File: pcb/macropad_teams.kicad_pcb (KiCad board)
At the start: 2 copper layers, 140 x 72.5 mm, 32 parts, among them J1 Conn_01x04, SW1 SW_Push, SW10 SW_Push, SW11 SW_Push, SW12 SW_Push, SW13 SW_Push, SW14 SW_Push, SW2 SW_Push, SW3 SW_Push, SW4 SW_Push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

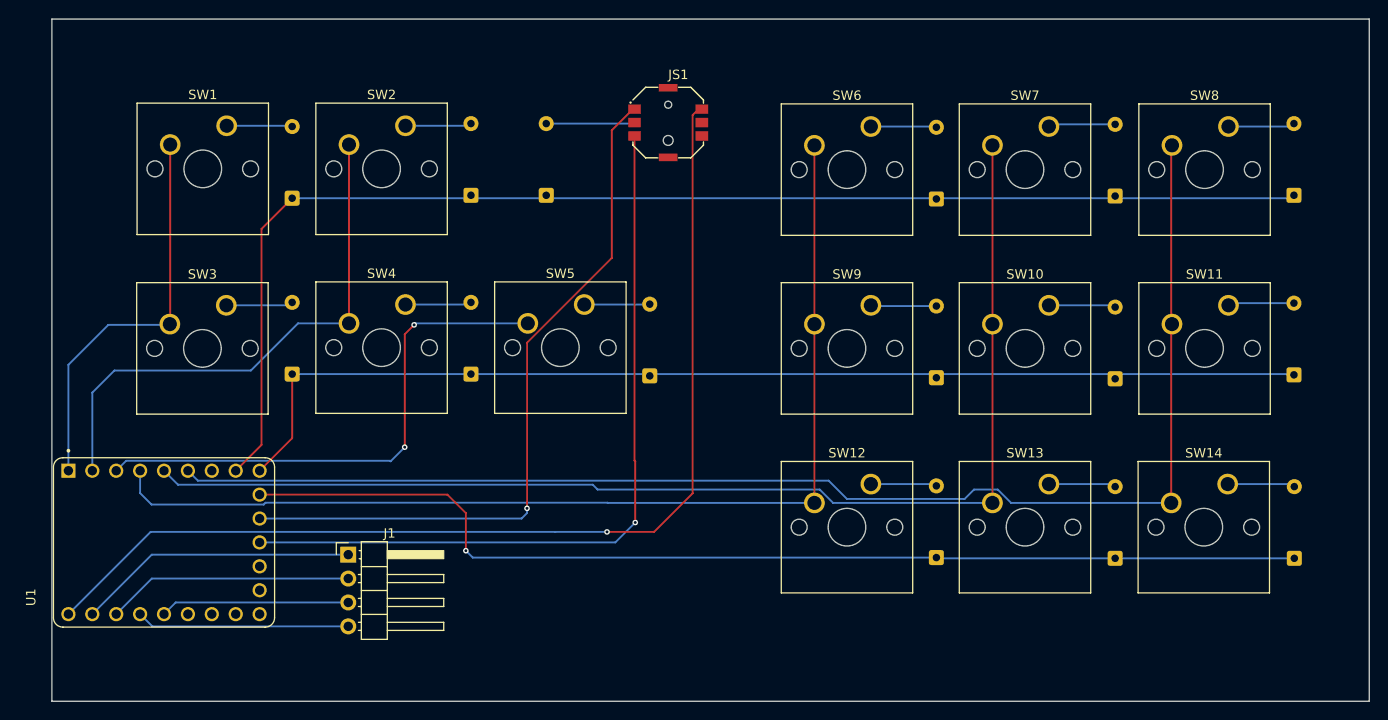
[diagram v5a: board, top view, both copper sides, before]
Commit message: On branch main Changes to be committed: 	deleted:    pcb/macropad_teams-backups/macropad_teams-2025-10-28_200539.zip 	deleted:    pcb/macropad_teams-backups/macropad_teams-2025-10-28_201254.zip 	deleted:    pcb/macropad_teams-backups/macropad_teams-2025-10-28_205726.zip 	modified:   pcb/macropad_teams.kicad_pcb 	modified:   pcb/macropad_teams.kicad_prl
Successfully connected all parts of the joystick to the other components, whereas before this commit, there was an unrouted net.
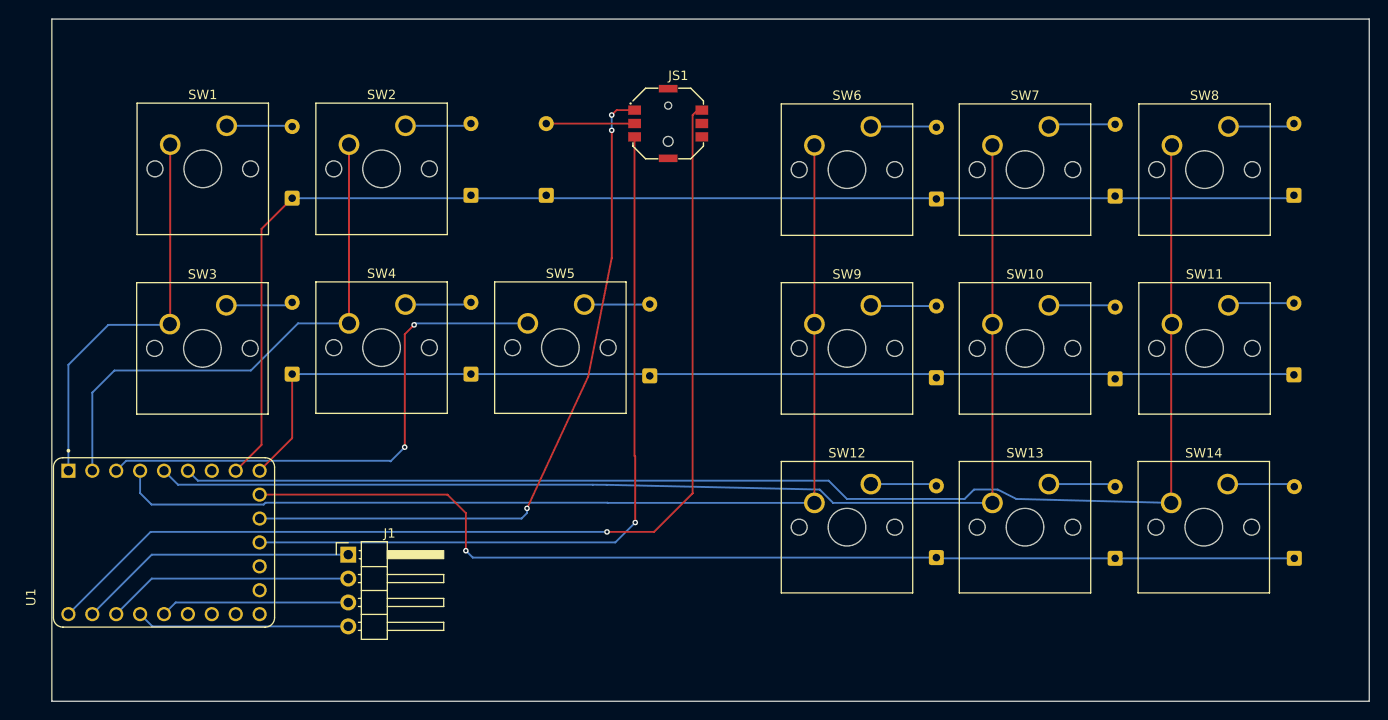
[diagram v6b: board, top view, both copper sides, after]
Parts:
- moved JS1 0.10 mm to (147.0, 71.1)
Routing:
- net /JS_X: track 76.4 -> 75.5 mm, vias 1 -> 3
- net Net-(D15-A): track 9.01 -> 9.66 mm
- net /JS_Y: track 81.9 -> 81.4 mm
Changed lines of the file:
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@@
 	(footprint "joy:SW_SKRHABE010_SMD"
 		(layer "F.Cu")
-		(at 147 71)
+		(at 147 71.1)
 		(property "Reference" "JS1"
 			(at 0 -4.5 0)
@@
 	)
 	(segment
-		(start 181.46 111.42)
-		(end 164.521314 111.42)
+		(start 164.521314 111.42)
+		(end 163.101314 110)
 		(width 0.2)
 		(layer "B.Cu")
@@
 	)
 	(segment
-		(start 138.985 109.485)
-		(end 94.905 109.485)
+		(start 140.5 109.5)
+		(end 138.985 109.485)
 		(width 0.2)
 		(layer "B.Cu")
@@
 	)
 	(segment
-		(start 164.521314 111.42)
-		(end 163.101314 110)
+		(start 163.101314 110)
+		(end 140.5 109.5)
 		(width 0.2)
 		(layer "B.Cu")
@@
 	)
 	(segment
-		(start 163.101314 110)
-		(end 139.5 110)
+		(start 138.985 109.485)
+		(end 94.905 109.485)
 		(width 0.2)
 		(layer "B.Cu")
@@
 	)
 	(segment
-		(start 139.5 110)
-		(end 138.985 109.485)
+		(start 181.46 111.42)
+		(end 164.521314 111.42)
 		(width 0.2)
 		(layer "B.Cu")
@@
 	)
 	(segment
-		(start 178.5 111)
-		(end 179.5 110)
+		(start 182.021314 110)
+		(end 184 111)
 		(width 0.2)
 		(layer "B.Cu")
@@
 	)
 	(segment
-		(start 164.055 109.055)
-		(end 166 111)
+		(start 95.96 108)
+		(end 97.015 109.055)
 		(width 0.2)
 		(layer "B.Cu")
@@
 	)
 	(segment
-		(start 166 111)
-		(end 178.5 111)
+		(start 178.5 111)
+		(end 179.5 110)
 		(width 0.2)
 		(layer "B.Cu")
@@
 	)
 	(segment
-		(start 182.021314 110)
-		(end 183.441314 111.42)
+		(start 164.055 109.055)
+		(end 166 111)
 		(width 0.2)
 		(layer "B.Cu")
@@
 	)
 	(segment
-		(start 183.441314 111.42)
+		(start 184 111)
 		(end 200.46 111.42)
 		(width 0.2)
@@
 	)
 	(segment
-		(start 95.96 108)
-		(end 97.015 109.055)
+		(start 97.015 109.055)
+		(end 164.055 109.055)
 		(width 0.2)
 		(layer "B.Cu")
@@
 	)
 	(segment
-		(start 97.015 109.055)
-		(end 164.055 109.055)
+		(start 166 111)
+		(end 178.5 111)
 		(width 0.2)
 		(layer "B.Cu")
@@
 	)
 	(segment
-		(start 143.425 106.925)
-		(end 143.5 107)
+		(start 143.425 106.425)
+		(end 143.425 72.925)
 		(width 0.2)
 		(layer "F.Cu")
@@
 	)
 	(segment
-		(start 143.5 107)
-		(end 143.5 113.5)
+		(start 143.5 106.5)
+		(end 143.425 106.425)
 		(width 0.2)
 		(layer "F.Cu")
@@
 	)
 	(segment
-		(start 143.425 72.425)
-		(end 143.425 106.925)
+		(start 143.5 113.5)
+		(end 143.5 106.5)
 		(width 0.2)
 		(layer "F.Cu")
@@
 	)
 	(segment
-		(start 141 71.825)
-		(end 143.25 69.575)
+		(start 132 112)
+		(end 138.5 98)
 		(width 0.2)
 		(layer "F.Cu")
@@
 	)
 	(segment
-		(start 132 94.401314)
+		(start 138.5 98)
 		(end 141 85.401314)
 		(width 0.2)
@@
 	)
 	(segment
-		(start 143.25 69.575)
-		(end 143.425 69.575)
+		(start 141.525 69.675)
+		(end 141 70.2)
+		(width 0.2)
+		(layer "F.Cu")
+		(net 36)
+	)
+	(segment
+		(start 143.425 69.675)
+		(end 141.525 69.675)
 		(width 0.2)
 		(layer "F.Cu")
@@
 	)
 	(segment
-		(start 132 94.401314)
-		(end 132 112)
+		(start 143.25 69.575)
+		(end 143.425 69.575)
 		(width 0.2)
 		(layer "F.Cu")
@@
 	)
 	(via
+		(at 141 70.2)
+		(size 0.6)
+		(drill 0.3)
+		(layers "F.Cu" "B.Cu")
+		(net 36)
+	)
+	(via
+		(at 141 71.825)
+		(size 0.6)
+		(drill 0.3)
+		(layers "F.Cu" "B.Cu")
+		(net 36)
+	)
+	(via
 		(at 132 112)
 		(size 0.6)
@@
 	)
 	(segment
+		(start 141 70.2)
+		(end 141 71.825)
+		(width 0.2)
+		(layer "B.Cu")
+		(net 36)
+	)
+	(segment
 		(start 131.42 113.08)
 		(end 132 112.5)
@@
 	)
 	(segment
-		(start 150.223 69.575)
-		(end 149.599 70.199)
+		(start 150.123 69.675)
+		(end 150.575 69.675)
 		(width 0.2)
 		(layer "F.Cu")
@@
 		(net 37)
 	)
+	(segment
+		(start 149.599 70.199)
+		(end 150.123 69.675)
+		(width 0.2)
+		(layer "F.Cu")
+		(net 37)
+	)
 	(via
 		(at 140.5 114.5)
@@
 	)
 	(segment
-		(start 83.26 123.24)
-		(end 92 114.5)
+		(start 92 114.5)
+		(end 140.5 114.5)
 		(width 0.2)
 		(layer "B.Cu")
@@
 	)
 	(segment
-		(start 92 114.5)
-		(end 135 114.5)
+		(start 83.26 123.24)
+		(end 92 114.5)
 		(width 0.2)
 		(layer "B.Cu")
@@
 	)
 	(segment
-		(start 135 114.5)
-		(end 140.5 114.5)
+		(start 143.425 71.1)
+		(end 143.3 71.1)
 		(width 0.2)
-		(layer "B.Cu")
-		(net 37)
+		(layer "F.Cu")
+		(net 38)
 	)
 	(segment
-		(start 143 71)
-		(end 142.89 71.11)
+		(start 143.29 71.11)
+		(end 134.04 71.11)
 		(width 0.2)
-		(layer "B.Cu")
+		(layer "F.Cu")
+		(net 38)
+	)
+	(segment
+		(start 143.3 71.1)
+		(end 143.29 71.11)
+		(width 0.2)
+		(layer "F.Cu")
+		(net 38)
+	)
+	(segment
+		(start 143.3 71.1)
+		(end 143.2 71.2)
+		(width 0.2)
+		(layer "F.Cu")
 		(net 38)
 	)
 	(segment
 		(start 134.04 71.11)
-		(end 142.89 71.11)
+		(end 134.13 71.2)
 		(width 0.2)
 		(layer "B.Cu")
